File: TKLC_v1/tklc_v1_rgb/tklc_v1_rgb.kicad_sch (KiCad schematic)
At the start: 187 parts, among them J1 UART breakout for extension b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, J2 Encoder breakout, SW1 CherryMX_LED, SW10 CherryMX_LED, SW11 CherryMX_LED, SW12 CherryMX_LED, SW13 CherryMX_LED, SW14 CherryMX_LED, SW15 CherryMX_LED, SW16 CherryMX_LED, SW17 RotaryEncoder_Switch, SW18 CherryMX_LED, SW19 CherryMX_LED, SW2 CherryMX_LED, SW20 CherryMX_LED, SW21 CherryMX_LED, SW22 CherryMX_LED, SW23 CherryMX_LED, SW24 CherryMX_LED, SW25 CherryMX_LED, SW26 CherryMX_LED, SW27 CherryMX_LED, SW28 CherryMX_LED, SW29 CherryMX_LED, SW3 CherryMX_LED, SW30 CherryMX_LED, SW31 CherryMX_LED, SW32 CherryMX_LED, SW33 CherryMX_LED, SW34 CherryMX_LED, SW35 CherryMX_LED, SW36 CherryMX_LED, SW37 CherryMX_LED, SW38 CherryMX_LED, SW39 CherryMX_LED, SW4 CherryMX_LED, SW40 CherryMX_LED, SW41 CherryMX_LED, SW42 CherryMX_LED, SW43 CherryMX_LED, SW44 CherryMX_LED, SW45 CherryMX_LED, SW46 CherryMX_LED, SW47 CherryMX_LED, SW48 CherryMX_LED, SW49 CherryMX_LED, SW5 CherryMX_LED, SW50 CherryMX_LED, SW51 CherryMX_LED, SW52 CherryMX_LED, SW53 CherryMX_LED, SW54 CherryMX_LED, SW55 CherryMX_LED, SW56 CherryMX_LED, SW57 CherryMX_LED, SW58 CherryMX_LED, SW59 CherryMX_LED, SW6 CherryMX_LED, SW60 CherryMX_LED, SW61 CherryMX_LED, SW62 CherryMX_LED, SW63 CherryMX_LED, SW64 CherryMX_LED, SW65 CherryMX_LED, SW66 CherryMX_LED, SW67 CherryMX_LED, SW68 CherryMX_LED, SW69 CherryMX_LED, SW7 CherryMX_LED, SW70 CherryMX_LED, SW71 CherryMX_LED, SW72 CherryMX_LED, SW73 CherryMX_LED, SW74 CherryMX_LED, SW75 CherryMX_LED, SW76 CherryMX_LED, SW77 CherryMX_LED, SW78 CherryMX_LED, SW79 CherryMX_LED, SW8 CherryMX_LED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

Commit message: Wired columns
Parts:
- added SW17b1: SW_Push, Button_Switch_THT:SW_PUSH_6mm, symbol Switch:SW_Push
- J1: footprint Connector:FanPinHeader_1x03_P2.54mm_Vertical -> Connector_PinHeader_2.54mm:PinHeader_1x03_P2.54mm_Horizontal
- J2: footprint Connector:FanPinHeader_1x04_P2.54mm_Vertical -> Connector_PinHeader_2.54mm:PinHeader_1x04_P2.54mm_Horizontal
- SW34, SW47: footprint edited_footprints:CMX-GLP_Hotswap_RGB_1.00u -> edited_footprints:CMX-GLP_Hotswap_RGB_1.50u
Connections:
- net col10: now also U1.19 (GP14); no longer U1.14 (GP10)
- net col11: now also U1.17 (GP13); no longer U1.15 (GP11)
- net col13: now also U1.15 (GP11); no longer U1.17 (GP13)
- net col14: now also U1.14 (GP10); no longer U1.19 (GP14)
- net col15: now also U1.12 (GP9); no longer U1.20 (GP15)
- net col16: now also SW17b1.1
- net col9: now also U1.20 (GP15); no longer U1.12 (GP9)
- net at D17.2 (A), SW17.S2: now also SW17b1.2
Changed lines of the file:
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@@
   (junction (at 97.79 121.92) (diameter 0) (color 0 0 0 0)
   )
+  (junction (at 563.88 52.07) (diameter 0) (color 0 0 0 0)
+  )
   (junction (at 231.14 106.68) (diameter 0) (color 0 0 0 0)
   )
@@
   (junction (at 81.28 186.69) (diameter 0) (color 0 0 0 0)
   )
+  (junction (at 561.34 59.69) (diameter 0) (color 0 0 0 0)
+  )
   (junction (at 414.02 68.58) (diameter 0) (color 0 0 0 0)
   )
@@
     (stroke (width 0) (type default) (color 0 0 0 0))
   )
+  (wire (pts (xy 568.96 49.53) (xy 563.88 49.53))
+    (stroke (width 0) (type default) (color 0 0 0 0))
+  )
   (wire (pts (xy 464.82 55.88) (xy 478.79 55.88))
     (stroke (width 0) (type default) (color 0 0 0 0))
@@
     (stroke (width 0) (type default) (color 0 0 0 0))
   )
+  (wire (pts (xy 561.34 59.69) (xy 561.34 60.96))
+    (stroke (width 0) (type default) (color 0 0 0 0))
+  )
   (wire (pts (xy 337.82 212.09) (xy 334.01 212.09))
     (stroke (width 0) (type default) (color 0 0 0 0))
@@
     (stroke (width 0) (type default) (color 0 0 0 0))
   )
+  (wire (pts (xy 563.88 49.53) (xy 563.88 52.07))
+    (stroke (width 0) (type default) (color 0 0 0 0))
+  )
   (wire (pts (xy 190.5 55.88) (xy 204.47 55.88))
     (stroke (width 0) (type default) (color 0 0 0 0))
@@
     (stroke (width 0) (type default) (color 0 0 0 0))
   )
-  (wire (pts (xy 561.34 60.96) (xy 561.34 57.15))
+  (wire (pts (xy 561.34 57.15) (xy 561.34 59.69))
     (stroke (width 0) (type default) (color 0 0 0 0))
   )
@@
     (stroke (width 0) (type default) (color 0 0 0 0))
   )
+  (wire (pts (xy 568.96 59.69) (xy 561.34 59.69))
+    (stroke (width 0) (type default) (color 0 0 0 0))
+  )
   (wire (pts (xy 420.37 156.21) (xy 420.37 154.94))
     (stroke (width 0) (type default) (color 0 0 0 0))
@@
     (effects (font (size 1.27 1.27)) (justify right bottom))
   )
-  (label "col10" (at 154.94 318.77 180)
+  (label "col10" (at 154.94 331.47 180)
     (effects (font (size 1.27 1.27)) (justify right bottom))
   )
@@
     (effects (font (size 1.27 1.27)) (justify right bottom))
   )
-  (label "col15" (at 154.94 334.01 180)
+  (label "col15" (at 154.94 313.69 180)
     (effects (font (size 1.27 1.27)) (justify right bottom))
   )
@@
     (effects (font (size 1.27 1.27)) (justify left bottom))
   )
-  (label "col14" (at 154.94 331.47 180)
+  (label "col14" (at 154.94 318.77 180)
     (effects (font (size 1.27 1.27)) (justify right bottom))
   )
-  (label "col11" (at 154.94 321.31 180)
+  (label "col11" (at 154.94 326.39 180)
     (effects (font (size 1.27 1.27)) (justify right bottom))
   )
@@
     (effects (font (size 4 4)) (justify right bottom))
   )
-  (label "col13" (at 154.94 326.39 180)
+  (label "col13" (at 154.94 321.31 180)
     (effects (font (size 1.27 1.27)) (justify right bottom))
   )
-  (label "col9" (at 154.94 313.69 180)
+  (label "col9" (at 154.94 334.01 180)
     (effects (font (size 1.27 1.27)) (justify right bottom))
   )
@@
     (property "Reference" "SW34" (id 0) (at 64.135 113.03 0))
     (property "Value" "CherryMX_LED" (id 1) (at 64.135 115.57 0))
-    (property "Footprint" "edited_footprints:CMX-GLP_Hotswap_RGB_1.00u" (id 2) (at 64.77 121.92 0)
+    (property "Footprint" "edited_footprints:CMX-GLP_Hotswap_RGB_1.50u" (id 2) (at 64.77 121.92 0)
       (effects (font (size 1.27 1.27)) hide)
     )
@@
       (effects (font (size 1.27 1.27)) (justify left))
     )
-    (property "Footprint" "Connector:FanPinHeader_1x03_P2.54mm_Vertical" (id 2) (at 238.76 351.79 0)
+    (property "Footprint" "Connector_PinHeader_2.54mm:PinHeader_1x03_P2.54mm_Horizontal" (id 2) (at 238.76 351.79 0)
       (effects (font (size 1.27 1.27)) hide)
     )
@@
     (pin "2")
   )
+  (symbol (lib_id "Switch:SW_Push") (at 568.96 54.61 270) (unit 1)
+    (in_bom yes) (on_board yes) (fields_autoplaced)
+    (property "Reference" "SW17b1" (id 0) (at 572.77 53.3399 90)
+      (effects (font (size 1.27 1.27)) (justify left))
+    )
+    (property "Value" "SW_Push" (id 1) (at 572.77 55.8799 90)
+      (effects (font (size 1.27 1.27)) (justify left))
+    )
+    (property "Footprint" "Button_Switch_THT:SW_PUSH_6mm" (id 2) (at 574.04 54.61 0)
+      (effects (font (size 1.27 1.27)) hide)
+    )
+    (property "Datasheet" "~" (id 3) (at 574.04 54.61 0)
+      (effects (font (size 1.27 1.27)) hide)
+    )
+    (pin "1")
+    (pin "2")
+  )
   (symbol (lib_id "Diode:1N4148") (at 78.74 64.77 90) (unit 1)
     (in_bom yes) (on_board yes) (fields_autoplaced)
@@
       (effects (font (size 1.27 1.27)) (justify left))
     )
-    (property "Footprint" "Connector:FanPinHeader_1x04_P2.54mm_Vertical" (id 2) (at 304.8 351.79 0)
+    (property "Footprint" "Connector_PinHeader_2.54mm:PinHeader_1x04_P2.54mm_Horizontal" (id 2) (at 304.8 351.79 0)
       (effects (font (size 1.27 1.27)) hide)
     )
@@
     (property "Reference" "SW47" (id 0) (at 475.615 113.03 0))
     (property "Value" "CherryMX_LED" (id 1) (at 475.615 115.57 0))
-    (property "Footprint" "edited_footprints:CMX-GLP_Hotswap_RGB_1.00u" (id 2) (at 476.25 121.92 0)
+    (property "Footprint" "edited_footprints:CMX-GLP_Hotswap_RGB_1.50u" (id 2) (at 476.25 121.92 0)
       (effects (font (size 1.27 1.27)) hide)
     )
@@
     )
     (path "/6e0498f8-b058-4cb4-bf6e-4525b7eb06c9"
-      (reference "J1") (unit 1) (value "UART breakout for extension board") (footprint "Connector:FanPinHeader_1x03_P2.54mm_Vertical")
+      (reference "J1") (unit 1) (value "UART breakout for extension board") (footprint "Connector_PinHeader_2.54mm:PinHeader_1x03_P2.54mm_Horizontal")
     )
     (path "/e7df68b9-005e-4356-8346-8977265c3f40"
-      (reference "J2") (unit 1) (value "Encoder breakout") (footprint "Connector:FanPinHeader_1x04_P2.54mm_Vertical")
+      (reference "J2") (unit 1) (value "Encoder breakout") (footprint "Connector_PinHeader_2.54mm:PinHeader_1x04_P2.54mm_Horizontal")
     )
     (path "/e0a839f9-cf09-452e-9626-0bc49a03f31f"
@@
       (reference "SW17") (unit 1) (value "RotaryEncoder_Switch") (footprint "edited_footprints:EDIT_RotaryEncoder_Alps_EC11E-Switch_Vertical_H20mm")
     )
+    (path "/bf233abb-c4f0-4ee3-94e6-5b61b67ba993"
+      (reference "SW17b1") (unit 1) (value "SW_Push") (footprint "Button_Switch_THT:SW_PUSH_6mm")
+    )
     (path "/e53f1e76-93cb-4963-ae9a-4ebb714db9c9"
       (reference "SW18") (unit 1) (value "CherryMX_LED") (footprint "edited_footprints:CMX-GLP_Hotswap_RGB_1.00u")
@@
     )
     (path "/41ddf282-f863-4a31-ac23-5171a3e7c7eb"
-      (reference "SW34") (unit 1) (value "CherryMX_LED") (footprint "edited_footprints:CMX-GLP_Hotswap_RGB_1.00u")
+      (reference "SW34") (unit 1) (value "CherryMX_LED") (footprint "edited_footprints:CMX-GLP_Hotswap_RGB_1.50u")
     )
     (path "/a0f5f467-2002-4f20-b13f-90086b733fa0"
@@
     )
     (path "/ef6c9bec-4a8c-4911-86ce-22ad74e16840"
-      (reference "SW47") (unit 1) (value "CherryMX_LED") (footprint "edited_footprints:CMX-GLP_Hotswap_RGB_1.00u")
+      (reference "SW47") (unit 1) (value "CherryMX_LED") (footprint "edited_footprints:CMX-GLP_Hotswap_RGB_1.50u")
     )
     (path "/86ebd34f-f0cd-49dc-bcb7-0c8ea6c4bb8e"

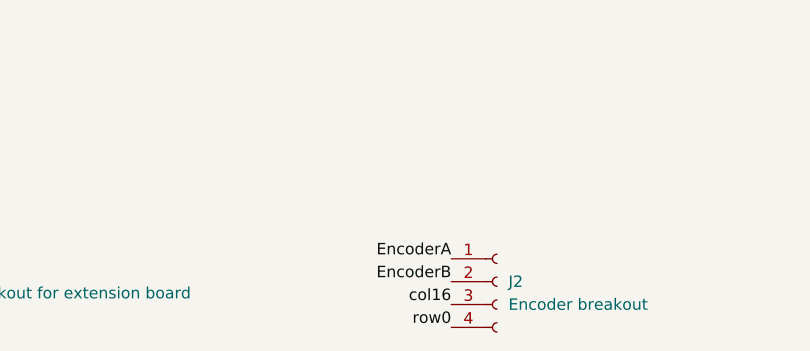
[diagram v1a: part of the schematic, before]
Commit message: Finished wiring everything but LED Power
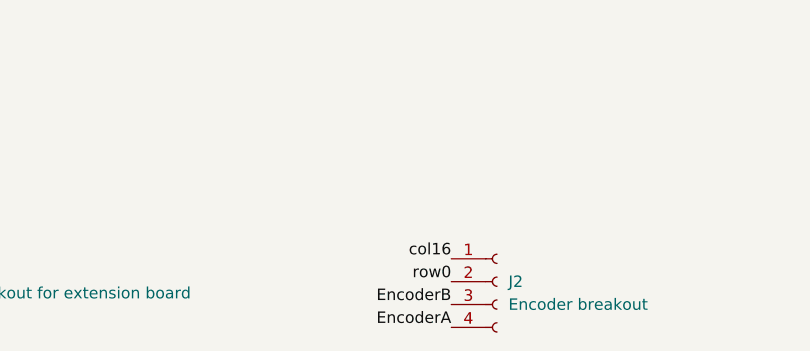
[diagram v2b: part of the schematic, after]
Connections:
- net EncoderA: now also J2.4 (Pin_4); no longer J2.1 (Pin_1)
- net EncoderB: now also J2.3 (Pin_3); no longer J2.2 (Pin_2)
- net col16: now also J2.1 (Pin_1); no longer J2.3 (Pin_3)
- net row0: now also J2.2 (Pin_2); no longer J2.4 (Pin_4)
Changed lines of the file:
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@@
     (effects (font (size 4 4)) (justify right bottom))
   )
-  (label "EncoderA" (at 299.72 349.25 180)
+  (label "EncoderA" (at 299.72 356.87 180)
     (effects (font (size 1.27 1.27)) (justify right bottom))
   )
@@
     (effects (font (size 1.27 1.27)) (justify left bottom))
   )
-  (label "EncoderB" (at 299.72 351.79 180)
+  (label "EncoderB" (at 299.72 354.33 180)
     (effects (font (size 1.27 1.27)) (justify right bottom))
   )
@@
     (effects (font (size 1.27 1.27)) (justify right bottom))
   )
-  (label "row0" (at 299.72 356.87 180)
+  (label "row0" (at 299.72 351.79 180)
     (effects (font (size 1.27 1.27)) (justify right bottom))
   )
@@
     (effects (font (size 1.27 1.27)) (justify right bottom))
   )
-  (label "col16" (at 299.72 354.33 180)
+  (label "col16" (at 299.72 349.25 180)
     (effects (font (size 1.27 1.27)) (justify right bottom))
   )

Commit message: Add files via upload
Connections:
- net PWR is gone; now on net RGB_PWR: SW80.3 (VDD), SW81.3 (VDD), SW82.3 (VDD), SW83.3 (VDD), SW84.3 (VDD), SW85.3 (VDD), SW86.3 (VDD), SW87.3 (VDD), SW88.3 (VDD), SW89.3 (VDD), SW90.3 (VDD), SW91.3 (VDD), SW92.3 (VDD)
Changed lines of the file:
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@@
     (effects (font (size 1.27 1.27)) (justify right bottom))
   )
-  (label "PWR" (at 39.37 228.6 180)
+  (label "RGB_PWR" (at 39.37 228.6 180)
     (effects (font (size 1.27 1.27)) (justify right bottom))
   )

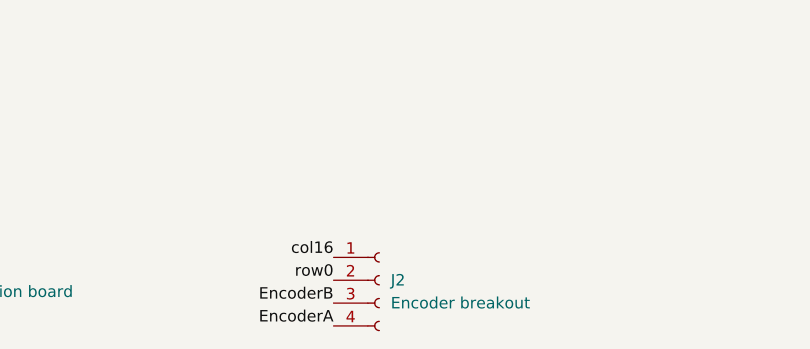
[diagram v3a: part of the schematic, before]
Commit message: FINISHED! Just need finishing touches
need to do rotary encoder button, art, and add teardrops and rounded corners.
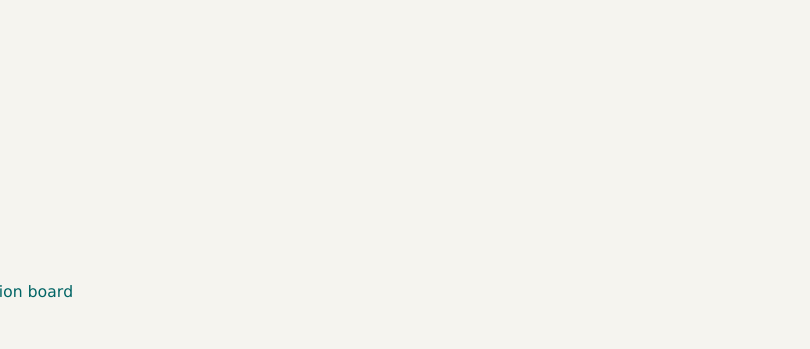
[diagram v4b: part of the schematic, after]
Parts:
- removed J2: Encoder breakout, Connector_PinHeader_2.54mm:PinHeader_1x04_P2.54mm_Horizontal, symbol Connector:Conn_01x04_Female
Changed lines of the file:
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@@
     (effects (font (size 4 4)) (justify right bottom))
   )
-  (label "EncoderA" (at 299.72 356.87 180)
-    (effects (font (size 1.27 1.27)) (justify right bottom))
-  )
   (label "row3" (at 210.82 313.69 0)
     (effects (font (size 1.27 1.27)) (justify left bottom))
@@
     (effects (font (size 1.27 1.27)) (justify left bottom))
   )
-  (label "EncoderB" (at 299.72 354.33 180)
-    (effects (font (size 1.27 1.27)) (justify right bottom))
-  )
   (label "col7" (at 279.4 22.86 180)
     (effects (font (size 4 4)) (justify right bottom))
@@
     (effects (font (size 1.27 1.27)) (justify right bottom))
   )
-  (label "row0" (at 299.72 351.79 180)
-    (effects (font (size 1.27 1.27)) (justify right bottom))
-  )
   (label "col14" (at 492.76 22.86 180)
     (effects (font (size 4 4)) (justify right bottom))
@@
     (effects (font (size 1.27 1.27)) (justify right bottom))
   )
-  (label "col16" (at 299.72 349.25 180)
-    (effects (font (size 1.27 1.27)) (justify right bottom))
-  )
   (label "RGB_PWR" (at 39.37 228.6 180)
     (effects (font (size 1.27 1.27)) (justify right bottom))
@@
     (pin "2")
   )
-  (symbol (lib_id "Connector:Conn_01x04_Female") (at 304.8 351.79 0) (unit 1)
-    (in_bom yes) (on_board yes) (fields_autoplaced)
-    (property "Reference" "J2" (id 0) (at 306.07 351.7899 0)
-      (effects (font (size 1.27 1.27)) (justify left))
-    )
-    (property "Value" "Encoder breakout" (id 1) (at 306.07 354.3299 0)
-      (effects (font (size 1.27 1.27)) (justify left))
-    )
-    (property "Footprint" "Connector_PinHeader_2.54mm:PinHeader_1x04_P2.54mm_Horizontal" (id 2) (at 304.8 351.79 0)
-      (effects (font (size 1.27 1.27)) hide)
-    )
-    (property "Datasheet" "~" (id 3) (at 304.8 351.79 0)
-      (effects (font (size 1.27 1.27)) hide)
-    )
-    (pin "1")
-    (pin "2")
-    (pin "3")
-    (pin "4")
-  )
   (symbol (lib_name "CherryMX_SK6812_59") (lib_id "Cherry MX EDITS:CherryMX_SK6812") (at 240.03 53.34 0) (unit 1)
     (in_bom yes) (on_board yes) (fields_autoplaced)
@@
       (reference "J1") (unit 1) (value "UART breakout for extension board") (footprint "Connector_PinHeader_2.54mm:PinHeader_1x03_P2.54mm_Horizontal")
     )
-    (path "/e7df68b9-005e-4356-8346-8977265c3f40"
-      (reference "J2") (unit 1) (value "Encoder breakout") (footprint "Connector_PinHeader_2.54mm:PinHeader_1x04_P2.54mm_Horizontal")
-    )
     (path "/e0a839f9-cf09-452e-9626-0bc49a03f31f"

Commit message: Generated Gerber files and ordered PCBs
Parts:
- added C1: 10uF, edited_footprints:Cap_4mm_Horizontal, symbol Device:C
- added C2: 22uF, edited_footprints:Cap_4mm_Horizontal, symbol Device:C
- added R1: 500R, Resistor_THT:R_Axial_DIN0204_L3.6mm_D1.6mm_P7.62mm_Horizontal, symbol Device:R
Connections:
- net VBUS is gone; now on net RGB_PWR: U1.40 (VBUS)
- net GND: now also C1.2, C2.2
- net RGB_DATA: now also R1.2; no longer U1.22 (GP17)
- net RGB_PWR: now also C1.1, C2.1; no longer U1.39 (VSYS)
- new net: R1.1, U1.22 (GP17)
- new net VSYS: U1.39 (VSYS)
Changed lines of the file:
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@@
   (junction (at 295.91 91.44) (diameter 0) (color 0 0 0 0)
   )
+  (junction (at 220.98 285.75) (diameter 0) (color 0 0 0 0)
+  )
   (junction (at 356.87 91.44) (diameter 0) (color 0 0 0 0)
   )
@@
   (junction (at 330.2 198.12) (diameter 0) (color 0 0 0 0)
   )
+  (junction (at 232.41 293.37) (diameter 0) (color 0 0 0 0)
+  )
   (junction (at 523.24 120.65) (diameter 0) (color 0 0 0 0)
   )
@@
   (junction (at 306.07 57.15) (diameter 0) (color 0 0 0 0)
   )
+  (junction (at 232.41 285.75) (diameter 0) (color 0 0 0 0)
+  )
   (junction (at 386.08 120.65) (diameter 0) (color 0 0 0 0)
   )
@@
     (stroke (width 0) (type default) (color 0 0 0 0))
   )
+  (wire (pts (xy 232.41 293.37) (xy 241.3 293.37))
+    (stroke (width 0) (type default) (color 0 0 0 0))
+  )
   (wire (pts (xy 275.59 92.71) (xy 281.94 92.71))
     (stroke (width 0) (type default) (color 0 0 0 0))
@@
     (stroke (width 0) (type default) (color 0 0 0 0))
   )
+  (wire (pts (xy 232.41 285.75) (xy 241.3 285.75))
+    (stroke (width 0) (type default) (color 0 0 0 0))
+  )
   (wire (pts (xy 563.88 168.91) (xy 49.53 168.91))
     (stroke (width 0) (type default) (color 0 0 0 0))
@@
     (stroke (width 0) (type default) (color 0 0 0 0))
   )
-  (wire (pts (xy 198.12 285.75) (xy 210.82 285.75))
+  (wire (pts (xy 198.12 285.75) (xy 220.98 285.75))
     (stroke (width 0) (type default) (color 0 0 0 0))
   )
@@
     (stroke (width 0) (type default) (color 0 0 0 0))
   )
+  (wire (pts (xy 220.98 293.37) (xy 232.41 293.37))
+    (stroke (width 0) (type default) (color 0 0 0 0))
+  )
   (wire (pts (xy 266.7 123.19) (xy 266.7 124.46))
     (stroke (width 0) (type default) (color 0 0 0 0))
@@
     (stroke (width 0) (type default) (color 0 0 0 0))
   )
+  (wire (pts (xy 220.98 285.75) (xy 232.41 285.75))
+    (stroke (width 0) (type default) (color 0 0 0 0))
+  )
   (wire (pts (xy 334.01 182.88) (xy 364.49 182.88))
     (stroke (width 0) (type default) (color 0 0 0 0))
@@
     (stroke (width 0) (type default) (color 0 0 0 0))
   )
-  (wire (pts (xy 245.11 308.61) (xy 252.73 308.61))
-    (stroke (width 0) (type default) (color 0 0 0 0))
-  )
   (wire (pts (xy 210.82 143.51) (xy 210.82 151.13))
     (stroke (width 0) (type default) (color 0 0 0 0))
@@
     (stroke (width 0) (type default) (color 0 0 0 0))
   )
-  (wire (pts (xy 198.12 331.47) (xy 210.82 331.47))
+  (wire (pts (xy 198.12 331.47) (xy 215.9 331.47))
     (stroke (width 0) (type default) (color 0 0 0 0))
   )
@@
     (effects (font (size 1.27 1.27)) (justify left bottom))
   )
-  (label "VSYS" (at 245.11 308.61 180)
-    (effects (font (size 1.27 1.27)) (justify right bottom))
-  )
   (label "col15" (at 154.94 313.69 180)
     (effects (font (size 1.27 1.27)) (justify right bottom))
@@
     (effects (font (size 1.27 1.27)) (justify right bottom))
   )
-  (label "RGB_PWR" (at 252.73 308.61 0)
+  (label "RGB_PWR" (at 241.3 285.75 0)
     (effects (font (size 1.27 1.27)) (justify left bottom))
   )
-  (label "RGB_DATA" (at 210.82 331.47 0)
+  (label "RGB_DATA" (at 223.52 331.47 0)
     (effects (font (size 1.27 1.27)) (justify left bottom))
   )
@@
     (effects (font (size 1.27 1.27)) (justify left bottom))
   )
-  (label "VBUS" (at 210.82 285.75 0)
-    (effects (font (size 1.27 1.27)) (justify left bottom))
-  )
   (label "LED_CONTROL" (at 210.82 326.39 0)
     (effects (font (size 1.27 1.27)) (justify left bottom))
@@
     (pin "6")
   )
+  (symbol (lib_id "Device:C") (at 220.98 289.56 0) (unit 1)
+    (in_bom yes) (on_board yes) (fields_autoplaced)
+    (property "Reference" "C1" (id 0) (at 224.79 288.2899 0)
+      (effects (font (size 1.27 1.27)) (justify left))
+    )
+    (property "Value" "10uF" (id 1) (at 224.79 290.8299 0)
+      (effects (font (size 1.27 1.27)) (justify left))
+    )
+    (property "Footprint" "edited_footprints:Cap_4mm_Horizontal" (id 2) (at 221.9452 293.37 0)
+      (effects (font (size 1.27 1.27)) hide)
+    )
+    (property "Datasheet" "~" (id 3) (at 220.98 289.56 0)
+      (effects (font (size 1.27 1.27)) hide)
+    )
+    (pin "1")
+    (pin "2")
+  )
   (symbol (lib_id "Cherry MX EDITS:CherryMX_SK6812") (at 95.25 213.36 0) (unit 1)
     (in_bom yes) (on_board yes) (fields_autoplaced)
@@
     (pin "6")
   )
+  (symbol (lib_id "Device:C") (at 232.41 289.56 0) (unit 1)
+    (in_bom yes) (on_board yes) (fields_autoplaced)
+    (property "Reference" "C2" (id 0) (at 236.22 288.2899 0)
+      (effects (font (size 1.27 1.27)) (justify left))
+    )
+    (property "Value" "22uF" (id 1) (at 236.22 290.8299 0)
+      (effects (font (size 1.27 1.27)) (justify left))
+    )
+    (property "Footprint" "edited_footprints:Cap_4mm_Horizontal" (id 2) (at 233.3752 293.37 0)
+      (effects (font (size 1.27 1.27)) hide)
+    )
+    (property "Datasheet" "~" (id 3) (at 232.41 289.56 0)
+      (effects (font (size 1.27 1.27)) hide)
+    )
+    (pin "1")
+    (pin "2")
+  )
   (symbol (lib_id "Diode:1N4148") (at 147.32 194.31 90) (unit 1)
     (in_bom yes) (on_board yes) (fields_autoplaced)
@@
     (pin "6")
   )
+  (symbol (lib_id "Device:R") (at 219.71 331.47 90) (unit 1)
+    (in_bom yes) (on_board yes) (fields_autoplaced)
+    (property "Reference" "R1" (id 0) (at 219.71 325.12 90))
+    (property "Value" "500R" (id 1) (at 219.71 327.66 90))
+    (property "Footprint" "Resistor_THT:R_Axial_DIN0204_L3.6mm_D1.6mm_P7.62mm_Horizontal" (id 2) (at 219.71 333.248 90)
+      (effects (font (size 1.27 1.27)) hide)
+    )
+    (property "Datasheet" "~" (id 3) (at 219.71 331.47 0)
+      (effects (font (size 1.27 1.27)) hide)
+    )
+    (pin "1")
+    (pin "2")
+  )
   (symbol (lib_id "Diode:1N4148") (at 353.06 102.87 90) (unit 1)
     (in_bom yes) (on_board yes) (fields_autoplaced)
@@
     (pin "6")
   )
+  (symbol (lib_id "power:GND") (at 241.3 293.37 0) (unit 1)
+    (in_bom yes) (on_board yes) (fields_autoplaced)
+    (property "Reference" "#PWR0103" (id 0) (at 241.3 299.72 0)
+      (effects (font (size 1.27 1.27)) hide)
+    )
+    (property "Value" "GND" (id 1) (at 241.3 298.45 0))
+    (property "Footprint" "" (id 2) (at 241.3 293.37 0)
+      (effects (font (size 1.27 1.27)) hide)
+    )
+    (property "Datasheet" "" (id 3) (at 241.3 293.37 0)
+      (effects (font (size 1.27 1.27)) hide)
+    )
+    (pin "1")
+  )
   (symbol (lib_id "Cherry MX EDITS:CherryMX_SK6812") (at 87.63 53.34 0) (unit 1)
     (in_bom yes) (on_board yes) (fields_autoplaced)
@@
       (reference "#PWR0102") (unit 1) (value "GND") (footprint "")
     )
+    (path "/73b735fe-2f5e-4789-a2de-c073493c4495"
+      (reference "#PWR0103") (unit 1) (value "GND") (footprint "")
+    )
+    (path "/2eadee72-3129-4584-a328-20901692c2a1"
+      (reference "C1") (unit 1) (value "10uF") (footprint "edited_footprints:Cap_4mm_Horizontal")
+    )
+    (path "/3503f2f2-90ad-44a2-8948-8bb3373618d4"
+      (reference "C2") (unit 1) (value "22uF") (footprint "edited_footprints:Cap_4mm_Horizontal")
+    )
     (path "/4d1c2f80-7475-470f-a322-222f85b99a36"
       (reference "D1") (unit 1) (value "1N4148") (footprint "edited_footprints:D_T-1_P5.08mm_Horizontal")
@@
       (reference "J1") (unit 1) (value "UART breakout for extension board") (footprint "Connector_PinHeader_2.54mm:PinHeader_1x03_P2.54mm_Horizontal")
     )
+    (path "/5f8f5ce1-ca1f-4990-90a5-d8df5fcea750"
+      (reference "R1") (unit 1) (value "500R") (footprint "Resistor_THT:R_Axial_DIN0204_L3.6mm_D1.6mm_P7.62mm_Horizontal")
+    )
     (path "/e0a839f9-cf09-452e-9626-0bc49a03f31f"
